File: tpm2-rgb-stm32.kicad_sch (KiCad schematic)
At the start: 58 parts, among them J1 Screw_Terminal_01x04, J2 Screw_Terminal_01x08, J3 Screw_Terminal_01x02, J4 Screw_Terminal_01x02, J5 12401832E402A, SW1 SW_Push, U1 COS4426SR, U10 IRF7458TRPBF, U11 IRF7458TRPBF, U12 COS4426SR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

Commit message: Touch things up
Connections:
- net PMW1 is gone; now on net PWM1: U4.38 (PA15)
- net GATE1: no longer U12.7 (NOUTA), U5.7 (NOUTA), U8.7 (NOUTA)
- net GATE2: no longer U12.5 (NOUTB), U5.5 (NOUTB), U8.5 (NOUTB)
- net GATE3: now also U5.7 (NOUTA)
- net GATE4: now also U5.5 (NOUTB)
- net GATE5: now also U8.7 (NOUTA)
- net GATE6: now also U8.5 (NOUTB)
- net GATE7: now also U12.7 (NOUTA)
- net GATE8: now also U12.5 (NOUTB)
- net OUT1: no longer U10.5 (D), U10.6 (D), U10.7 (D), U10.8 (D), U13.5 (D), U13.6 (D), U13.7 (D), U13.8 (D), U6.5 (D), U6.6 (D), U6.7 (D), U6.8 (D)
- net OUT2: no longer U11.5 (D), U11.6 (D), U11.7 (D), U11.8 (D), U14.5 (D), U14.6 (D), U14.7 (D), U14.8 (D), U7.5 (D), U7.6 (D), U7.7 (D), U7.8 (D)
- net OUT3: now also U6.5 (D), U6.6 (D), U6.7 (D), U6.8 (D)
- net OUT4: now also U7.5 (D), U7.6 (D), U7.7 (D), U7.8 (D)
- net OUT5: now also U10.5 (D), U10.6 (D), U10.7 (D), U10.8 (D)
- net OUT6: now also U11.5 (D), U11.6 (D), U11.7 (D), U11.8 (D)
- net OUT7: now also U13.5 (D), U13.6 (D), U13.7 (D), U13.8 (D)
- net OUT8: now also U14.5 (D), U14.6 (D), U14.7 (D), U14.8 (D)
- net PWM1: no longer U1.4 (INB), U12.2 (INA), U12.4 (INB), U5.2 (INA), U5.4 (INB), U8.2 (INA), U8.4 (INB)
- net PMW2 renamed PWM2
- net PWM2: now also U1.4 (INB)
- net PMW3 renamed PWM3
- net PWM3: now also U5.2 (INA)
- net PMW4 renamed PWM4
- net PWM4: now also U5.4 (INB)
- net PMW5 renamed PWM5
- net PWM5: now also U8.2 (INA)
- net PMW6 renamed PWM6
- net PWM6: now also U8.4 (INB)
- net PMW7 renamed PWM7
- net PWM7: now also U12.2 (INA)
- net PMW8 renamed PWM8
- net PWM8: now also U12.4 (INB)
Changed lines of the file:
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@@
     (effects (font (size 1.27 1.27)) (justify left bottom))
   )
-  (global_label "PWM1" (shape input) (at 123.19 187.96 180) (fields_autoplaced)
+  (global_label "PWM4" (shape input) (at 123.19 187.96 180) (fields_autoplaced)
     (effects (font (size 1.27 1.27)) (justify right))
     (property "Intersheet References" "${INTERSHEET_REFS}" (id 0) (at 115.3945 187.8806 0)
@@
     )
   )
-  (global_label "GATE1" (shape input) (at 161.29 177.8 0) (fields_autoplaced)
+  (global_label "GATE3" (shape input) (at 161.29 177.8 0) (fields_autoplaced)
     (effects (font (size 1.27 1.27)) (justify left))
     (property "Intersheet References" "${INTERSHEET_REFS}" (id 0) (at 169.3879 177.7206 0)
@@
     )
   )
-  (global_label "OUT2" (shape input) (at 280.67 232.41 0) (fields_autoplaced)
+  (global_label "OUT6" (shape input) (at 280.67 232.41 0) (fields_autoplaced)
     (effects (font (size 1.27 1.27)) (justify left))
     (property "Intersheet References" "${INTERSHEET_REFS}" (id 0) (at 287.9212 232.3306 0)
@@
     )
   )
-  (global_label "PWM1" (shape input) (at 123.19 177.8 180) (fields_autoplaced)
+  (global_label "PWM3" (shape input) (at 123.19 177.8 180) (fields_autoplaced)
     (effects (font (size 1.27 1.27)) (justify right))
     (property "Intersheet References" "${INTERSHEET_REFS}" (id 0) (at 115.3945 177.7206 0)
@@
     )
   )
-  (global_label "PMW2" (shape input) (at 193.04 124.46 180) (fields_autoplaced)
+  (global_label "PWM2" (shape input) (at 193.04 124.46 180) (fields_autoplaced)
     (effects (font (size 1.27 1.27)) (justify right))
     (property "Intersheet References" "${INTERSHEET_REFS}" (id 0) (at 185.2445 124.3806 0)
@@
     )
   )
-  (global_label "OUT2" (shape input) (at 161.29 232.41 0) (fields_autoplaced)
+  (global_label "OUT4" (shape input) (at 161.29 232.41 0) (fields_autoplaced)
     (effects (font (size 1.27 1.27)) (justify left))
     (property "Intersheet References" "${INTERSHEET_REFS}" (id 0) (at 168.5412 232.3306 0)
@@
     )
   )
-  (global_label "OUT1" (shape input) (at 280.67 209.55 0) (fields_autoplaced)
+  (global_label "OUT5" (shape input) (at 280.67 209.55 0) (fields_autoplaced)
     (effects (font (size 1.27 1.27)) (justify left))
     (property "Intersheet References" "${INTERSHEET_REFS}" (id 0) (at 287.9212 209.4706 0)
@@
     )
   )
-  (global_label "PMW7" (shape input) (at 193.04 116.84 180) (fields_autoplaced)
+  (global_label "PWM7" (shape input) (at 193.04 116.84 180) (fields_autoplaced)
     (effects (font (size 1.27 1.27)) (justify right))
     (property "Intersheet References" "${INTERSHEET_REFS}" (id 0) (at 185.2445 116.7606 0)
@@
     )
   )
-  (global_label "GATE2" (shape input) (at 365.76 185.42 0) (fields_autoplaced)
+  (global_label "GATE8" (shape input) (at 365.76 185.42 0) (fields_autoplaced)
     (effects (font (size 1.27 1.27)) (justify left))
     (property "Intersheet References" "${INTERSHEET_REFS}" (id 0) (at 373.8579 185.3406 0)
@@
     )
   )
-  (global_label "PWM1" (shape input) (at 327.66 185.42 180) (fields_autoplaced)
+  (global_label "PWM8" (shape input) (at 327.66 185.42 180) (fields_autoplaced)
     (effects (font (size 1.27 1.27)) (justify right))
     (property "Intersheet References" "${INTERSHEET_REFS}" (id 0) (at 319.8645 185.3406 0)
@@
     )
   )
-  (global_label "GATE1" (shape input) (at 276.86 177.8 0) (fields_autoplaced)
+  (global_label "GATE5" (shape input) (at 276.86 177.8 0) (fields_autoplaced)
     (effects (font (size 1.27 1.27)) (justify left))
     (property "Intersheet References" "${INTERSHEET_REFS}" (id 0) (at 284.9579 177.7206 0)
@@
     )
   )
-  (global_label "PMW4" (shape input) (at 226.06 124.46 0) (fields_autoplaced)
+  (global_label "PWM4" (shape input) (at 226.06 124.46 0) (fields_autoplaced)
     (effects (font (size 1.27 1.27)) (justify left))
     (property "Intersheet References" "${INTERSHEET_REFS}" (id 0) (at 233.8555 124.3806 0)
@@
     )
   )
-  (global_label "PWM1" (shape input) (at 238.76 177.8 180) (fields_autoplaced)
+  (global_label "PWM5" (shape input) (at 238.76 177.8 180) (fields_autoplaced)
     (effects (font (size 1.27 1.27)) (justify right))
     (property "Intersheet References" "${INTERSHEET_REFS}" (id 0) (at 230.9645 177.7206 0)
@@
     )
   )
-  (global_label "PMW5" (shape input) (at 226.06 132.08 0) (fields_autoplaced)
+  (global_label "PWM5" (shape input) (at 226.06 132.08 0) (fields_autoplaced)
     (effects (font (size 1.27 1.27)) (justify left))
     (property "Intersheet References" "${INTERSHEET_REFS}" (id 0) (at 233.8555 132.0006 0)
@@
     )
   )
-  (global_label "PMW1" (shape input) (at 226.06 154.94 0) (fields_autoplaced)
+  (global_label "PWM1" (shape input) (at 226.06 154.94 0) (fields_autoplaced)
     (effects (font (size 1.27 1.27)) (justify left))
     (property "Intersheet References" "${INTERSHEET_REFS}" (id 0) (at 233.8555 154.8606 0)
@@
     )
   )
-  (global_label "PWM1" (shape input) (at 34.29 190.5 180) (fields_autoplaced)
+  (global_label "PWM2" (shape input) (at 34.29 190.5 180) (fields_autoplaced)
     (effects (font (size 1.27 1.27)) (justify right))
     (property "Intersheet References" "${INTERSHEET_REFS}" (id 0) (at 26.4945 190.4206 0)
@@
     )
   )
-  (global_label "GATE2" (shape input) (at 276.86 187.96 0) (fields_autoplaced)
+  (global_label "GATE6" (shape input) (at 276.86 187.96 0) (fields_autoplaced)
     (effects (font (size 1.27 1.27)) (justify left))
     (property "Intersheet References" "${INTERSHEET_REFS}" (id 0) (at 284.9579 187.8806 0)
@@
     )
   )
-  (global_label "PWM1" (shape input) (at 327.66 175.26 180) (fields_autoplaced)
+  (global_label "PWM7" (shape input) (at 327.66 175.26 180) (fields_autoplaced)
     (effects (font (size 1.27 1.27)) (justify right))
     (property "Intersheet References" "${INTERSHEET_REFS}" (id 0) (at 319.8645 175.1806 0)
@@
     )
   )
-  (global_label "OUT1" (shape input) (at 368.3 209.55 0) (fields_autoplaced)
+  (global_label "OUT7" (shape input) (at 368.3 209.55 0) (fields_autoplaced)
     (effects (font (size 1.27 1.27)) (justify left))
     (property "Intersheet References" "${INTERSHEET_REFS}" (id 0) (at 375.5512 209.4706 0)
@@
     )
   )
-  (global_label "GATE2" (shape input) (at 161.29 187.96 0) (fields_autoplaced)
+  (global_label "GATE4" (shape input) (at 161.29 187.96 0) (fields_autoplaced)
     (effects (font (size 1.27 1.27)) (justify left))
     (property "Intersheet References" "${INTERSHEET_REFS}" (id 0) (at 169.3879 187.8806 0)
@@
     )
   )
-  (global_label "OUT1" (shape input) (at 161.29 209.55 0) (fields_autoplaced)
+  (global_label "OUT3" (shape input) (at 161.29 209.55 0) (fields_autoplaced)
     (effects (font (size 1.27 1.27)) (justify left))
     (property "Intersheet References" "${INTERSHEET_REFS}" (id 0) (at 168.5412 209.4706 0)
@@
     )
   )
-  (global_label "PMW3" (shape input) (at 226.06 121.92 0) (fields_autoplaced)
+  (global_label "PWM3" (shape input) (at 226.06 121.92 0) (fields_autoplaced)
     (effects (font (size 1.27 1.27)) (justify left))
     (property "Intersheet References" "${INTERSHEET_REFS}" (id 0) (at 233.8555 121.8406 0)
@@
     )
   )
-  (global_label "PMW8" (shape input) (at 193.04 119.38 180) (fields_autoplaced)
+  (global_label "PWM8" (shape input) (at 193.04 119.38 180) (fields_autoplaced)
     (effects (font (size 1.27 1.27)) (justify right))
     (property "Intersheet References" "${INTERSHEET_REFS}" (id 0) (at 185.2445 119.3006 0)
@@
     )
   )
-  (global_label "PMW6" (shape input) (at 226.06 134.62 0) (fields_autoplaced)
+  (global_label "PWM6" (shape input) (at 226.06 134.62 0) (fields_autoplaced)
     (effects (font (size 1.27 1.27)) (justify left))
     (property "Intersheet References" "${INTERSHEET_REFS}" (id 0) (at 233.8555 134.5406 0)
@@
     )
   )
-  (global_label "PWM1" (shape input) (at 238.76 187.96 180) (fields_autoplaced)
+  (global_label "PWM6" (shape input) (at 238.76 187.96 180) (fields_autoplaced)
     (effects (font (size 1.27 1.27)) (justify right))
     (property "Intersheet References" "${INTERSHEET_REFS}" (id 0) (at 230.9645 187.8806 0)
@@
     )
   )
-  (global_label "GATE1" (shape input) (at 365.76 175.26 0) (fields_autoplaced)
+  (global_label "GATE7" (shape input) (at 365.76 175.26 0) (fields_autoplaced)
     (effects (font (size 1.27 1.27)) (justify left))
     (property "Intersheet References" "${INTERSHEET_REFS}" (id 0) (at 373.8579 175.1806 0)
@@
     )
   )
-  (global_label "OUT2" (shape input) (at 368.3 232.41 0) (fields_autoplaced)
+  (global_label "OUT8" (shape input) (at 368.3 232.41 0) (fields_autoplaced)
     (effects (font (size 1.27 1.27)) (justify left))
     (property "Intersheet References" "${INTERSHEET_REFS}" (id 0) (at 375.5512 232.3306 0)

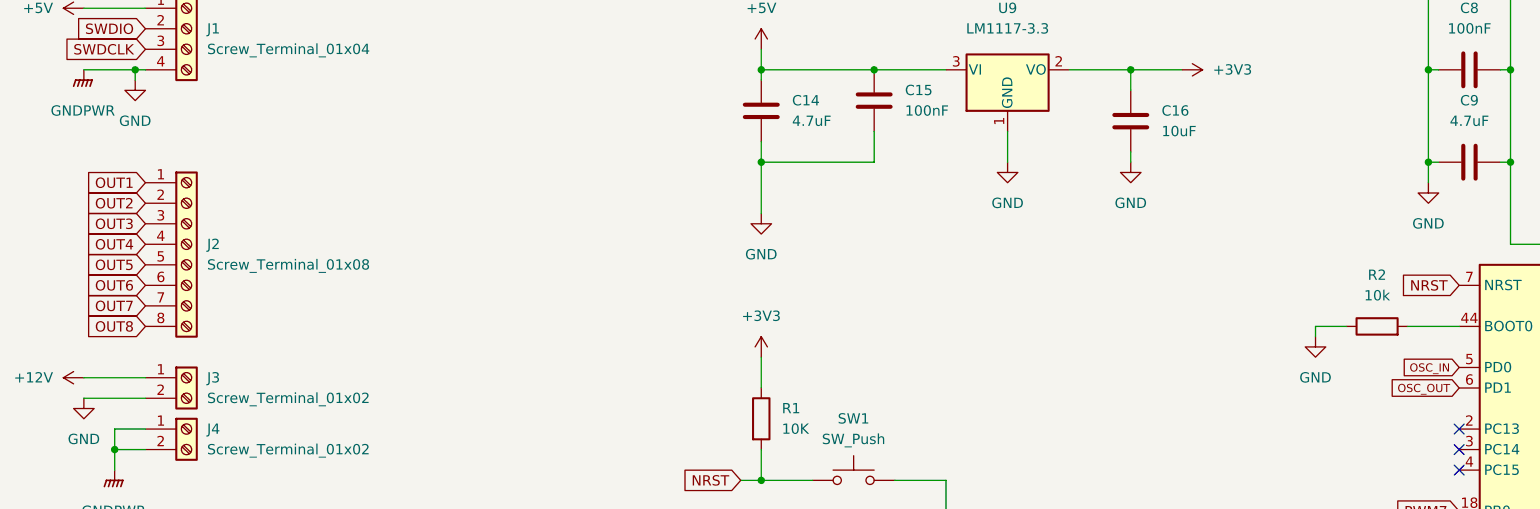
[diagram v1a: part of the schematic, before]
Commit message: Add missing footprints
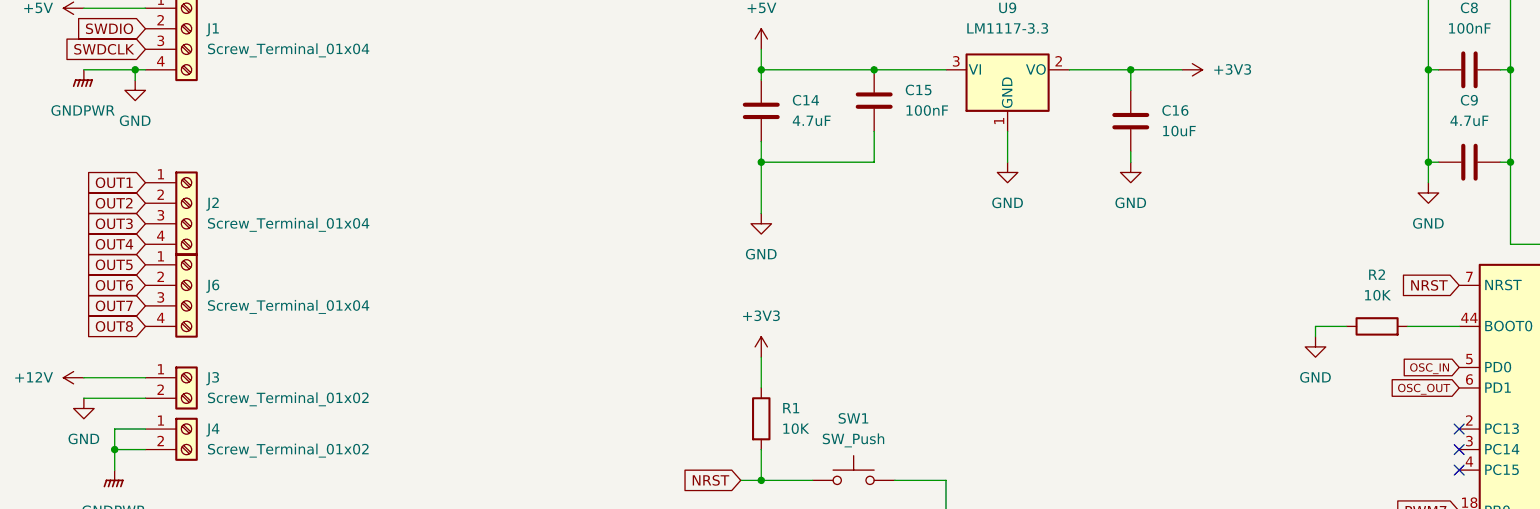
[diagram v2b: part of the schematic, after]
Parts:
- removed J2: Screw_Terminal_01x08, symbol Connector:Screw_Terminal_01x08
- added J2, J6: Screw_Terminal_01x04, TerminalBlock:TerminalBlock_bornier-4_P5.08mm, symbol Connector:Screw_Terminal_01x04
- C1, C10, C11, C12, C13, C14, C15, C16, C17, C18, C19, C2, C20, C21, C22, C23, C3, C4, C5, C6, C7, C8, C9: footprint (none) -> Capacitor_SMD:C_0805_2012Metric
- J1: footprint (none) -> TerminalBlock:TerminalBlock_bornier-4_P5.08mm
- J3, J4: footprint (none) -> TerminalBlock:TerminalBlock_bornier-2_P5.08mm
- J5: footprint AMPHENOL_12401832E402A -> 12401832E402A:AMPHENOL_12401832E402A
- R1, R10, R11, R12, R13, R3, R4, R5, R6, R7, R8, R9: footprint (none) -> Resistor_SMD:R_0805_2012Metric
- R2: value 10k -> 10K; footprint (none) -> Resistor_SMD:R_0805_2012Metric
- SW1: footprint (none) -> 147873-1:SW_147873-1
- U1, U12, U5, U8: footprint (none) -> Package_SO:SO-8_3.9x4.9mm_P1.27mm
- U10, U11, U13, U14, U2, U3, U6, U7: footprint SOIC127P490X600X175-8N -> IRF7458TRPBF:SOIC127P490X600X175-8N
- U9: footprint (none) -> Package_TO_SOT_SMD:SOT-223-3_TabPin2
- Y1: footprint (none) -> Crystal:Crystal_SMD_HC49-SD
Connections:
- net OUT1: now also J2.1 (Pin_1)
- net OUT2: now also J2.2 (Pin_2)
- net OUT3: now also J2.3 (Pin_3)
- net OUT4: now also J2.4 (Pin_4)
- net OUT5: now also J6.1 (Pin_1)
- net OUT6: now also J6.2 (Pin_2)
- net OUT7: now also J6.3 (Pin_3)
- net OUT8: now also J6.4 (Pin_4)

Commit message: Start layout
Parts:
- removed J1: Screw_Terminal_01x04, TerminalBlock:TerminalBlock_bornier-4_P5.08mm, symbol Connector:Screw_Terminal_01x04
- added J1: Conn_01x04_Male, Connector_PinHeader_2.54mm:PinHeader_1x04_P2.54mm_Vertical, symbol Connector:Conn_01x04_Male
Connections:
- net +5V: now also J1.4 (Pin_4)
- net GND: now also J1.1 (Pin_1)
- net SWDCLK: now also J1.2 (Pin_2)
- net SWDIO: now also J1.3 (Pin_3)
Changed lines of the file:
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@@
     (pin "1")
-  )
-  (symbol (lib_id "Connector:Screw_Terminal_01x04") (at 35.56 57.15 0) (unit 1)
-    (in_bom yes) (on_board yes) (fields_autoplaced)
-    (property "Reference" "J1" (id 0) (at 38.1 57.1499 0)
-      (effects (font (size 1.27 1.27)) (justify left))
-    )
-    (property "Value" "Screw_Terminal_01x04" (id 1) (at 38.1 59.6899 0)
-      (effects (font (size 1.27 1.27)) (justify left))
-    )
-    (property "Footprint" "TerminalBlock:TerminalBlock_bornier-4_P5.08mm" (id 2) (at 35.56 57.15 0)
-      (effects (font (size 1.27 1.27)) hide)
-    )
-    (property "Datasheet" "~" (id 3) (at 35.56 57.15 0)
-      (effects (font (size 1.27 1.27)) hide)
-    )
-    (pin "1")
-    (pin "2")
-    (pin "3")
-    (pin "4")
   )
   (symbol (lib_id "Connector:Screw_Terminal_01x02") (at 35.56 106.68 0) (unit 1)
@@
     )
     (pin "1")
+  )
+  (symbol (lib_id "Connector:Conn_01x04_Male") (at 35.56 59.69 180) (unit 1)
+    (in_bom yes) (on_board yes) (fields_autoplaced)
+    (property "Reference" "J1" (id 0) (at 36.83 57.1499 0)
+      (effects (font (size 1.27 1.27)) (justify right))
+    )
+    (property "Value" "Conn_01x04_Male" (id 1) (at 36.83 59.6899 0)
+      (effects (font (size 1.27 1.27)) (justify right))
+    )
+    (property "Footprint" "Connector_PinHeader_2.54mm:PinHeader_1x04_P2.54mm_Vertical" (id 2) (at 35.56 59.69 0)
+      (effects (font (size 1.27 1.27)) hide)
+    )
+    (property "Datasheet" "~" (id 3) (at 35.56 59.69 0)
+      (effects (font (size 1.27 1.27)) hide)
+    )
+    (pin "1")
+    (pin "2")
+    (pin "3")
+    (pin "4")
   )
   (symbol (lib_id "power:GND") (at 297.18 153.67 0) (unit 1)
@@
       (reference "C23") (unit 1) (value "1uF") (footprint "Capacitor_SMD:C_0805_2012Metric")
     )
-    (path "/76ac8801-96c2-4d1f-8895-83b364e5d482"
-      (reference "J1") (unit 1) (value "Screw_Terminal_01x04") (footprint "TerminalBlock:TerminalBlock_bornier-4_P5.08mm")
+    (path "/907cd329-c1ff-4b0e-af3c-bc66c755d479"
+      (reference "J1") (unit 1) (value "Conn_01x04_Male") (footprint "Connector_PinHeader_2.54mm:PinHeader_1x04_P2.54mm_Vertical")
     )
     (path "/c4da646a-d5a3-4fa8-9e7f-78ffdc65e3cd"

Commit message: Do more routing
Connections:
- net USDM is gone; now on net USBDM: U15.16 (USBD-)
- net USDP is gone; now on net USBDP: U15.15 (USBD+)
- net USBDN renamed USBDM
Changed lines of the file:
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@@
     )
   )
-  (global_label "USBDN" (shape input) (at 336.55 132.08 0) (fields_autoplaced)
-    (effects (font (size 1.27 1.27)) (justify left))
-    (property "Intersheet References" "${INTERSHEET_REFS}" (id 0) (at 345.3736 132.0006 0)
+  (global_label "USBDM" (shape input) (at 336.55 132.08 0) (fields_autoplaced)
+    (effects (font (size 1.27 1.27)) (justify left))
+    (property "Intersheet References" "${INTERSHEET_REFS}" (id 0) (at 345.4945 132.0006 0)
       (effects (font (size 1.27 1.27)) (justify left) hide)
     )
@@
     )
   )
-  (global_label "USDP" (shape input) (at 298.45 57.15 180) (fields_autoplaced)
-    (effects (font (size 1.27 1.27)) (justify right))
-    (property "Intersheet References" "${INTERSHEET_REFS}" (id 0) (at 290.9569 57.0706 0)
+  (global_label "USBDP" (shape input) (at 298.45 57.15 180) (fields_autoplaced)
+    (effects (font (size 1.27 1.27)) (justify right))
+    (property "Intersheet References" "${INTERSHEET_REFS}" (id 0) (at 289.6869 57.0706 0)
       (effects (font (size 1.27 1.27)) (justify right) hide)
     )
@@
     )
   )
-  (global_label "USBDN" (shape input) (at 300.99 134.62 180) (fields_autoplaced)
-    (effects (font (size 1.27 1.27)) (justify right))
-    (property "Intersheet References" "${INTERSHEET_REFS}" (id 0) (at 292.1664 134.5406 0)
+  (global_label "USBDM" (shape input) (at 300.99 134.62 180) (fields_autoplaced)
+    (effects (font (size 1.27 1.27)) (justify right))
+    (property "Intersheet References" "${INTERSHEET_REFS}" (id 0) (at 292.0455 134.5406 0)
       (effects (font (size 1.27 1.27)) (justify right) hide)
     )
@@
     )
   )
-  (global_label "USDM" (shape input) (at 298.45 59.69 180) (fields_autoplaced)
-    (effects (font (size 1.27 1.27)) (justify right))
-    (property "Intersheet References" "${INTERSHEET_REFS}" (id 0) (at 290.7755 59.6106 0)
-      (effects (font (size 1.27 1.27)) (justify right) hide)
-    )
+  (global_label "USBDM" (shape input) (at 298.45 59.69 180) (fields_autoplaced)
+    (effects (font (size 1.27 1.27)) (justify right))
+    (property "Intersheet References" "${INTERSHEET_REFS}" (id 0) (at 289.5055 59.6106 0)
+      (effects (font (size 1.27 1.27)) (justify right) hide)
+    )
